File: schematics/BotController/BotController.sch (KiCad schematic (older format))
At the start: 15 parts, among them IC1 ATMEGA644-P, SW2 reset, X1 CRYSTAL_OSSCI

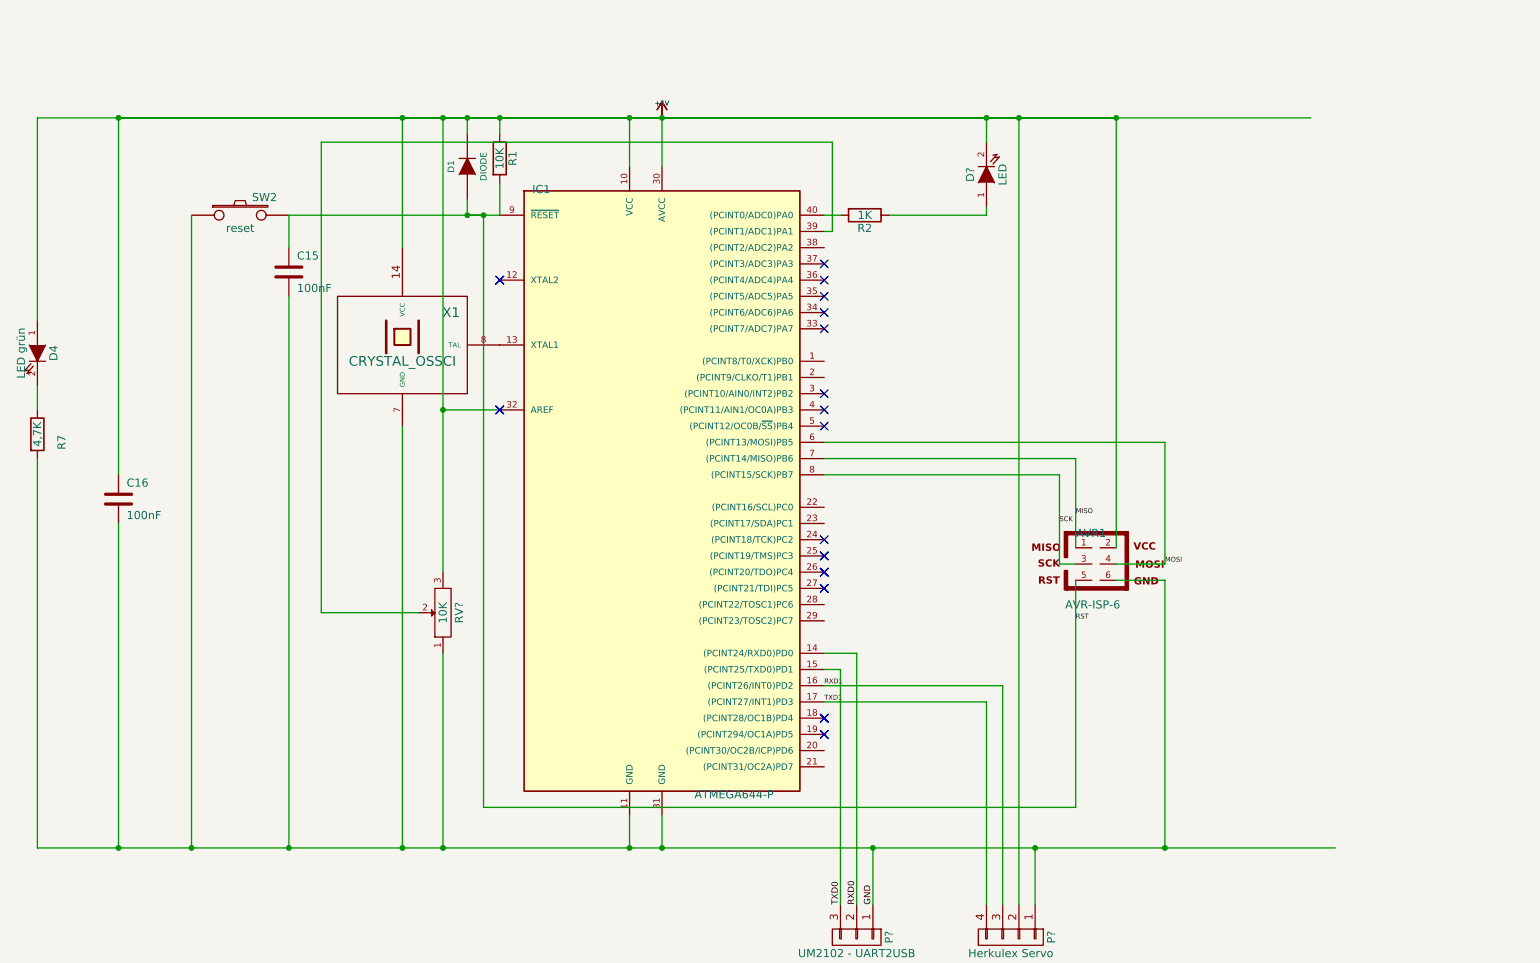
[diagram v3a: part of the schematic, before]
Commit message: Rotary Encoder mit gleicher I2c Adresse angesprochen
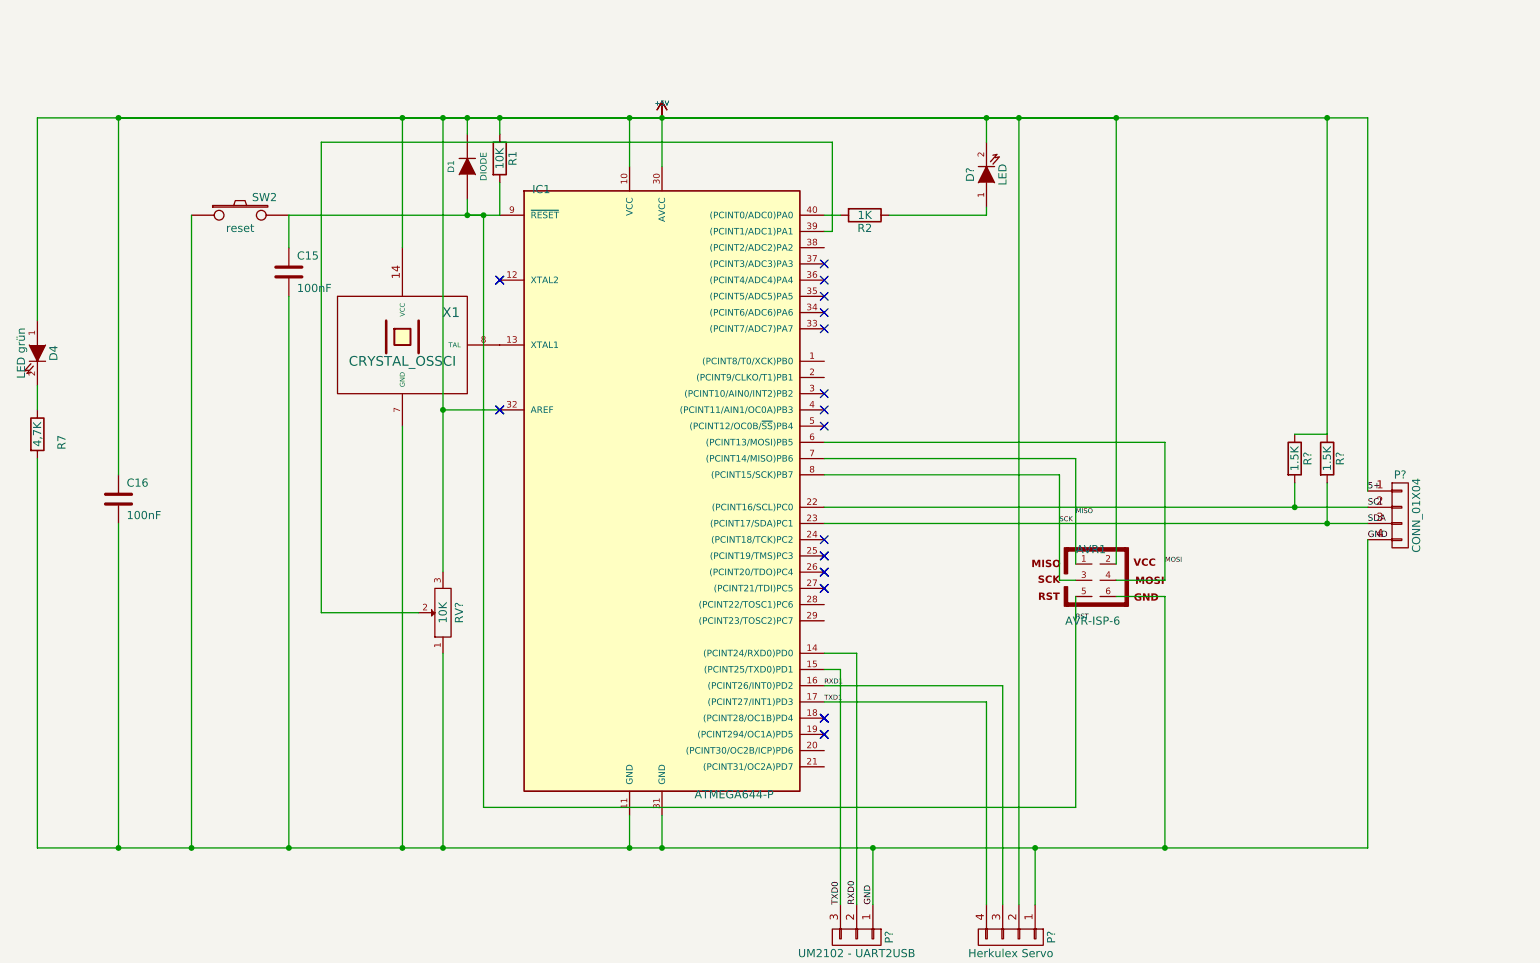
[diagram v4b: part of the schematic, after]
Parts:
- added P?: CONN_01X04, symbol CONN_01X04
- added R? (x2): 1.5K, symbol R
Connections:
- net labels added: 5+, SCl, SDA
- wire segments 63 -> 105
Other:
- moved on the sheet: AVR1
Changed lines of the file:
@@
 	2750 2300 2750 2500
 Wire Wire Line
-	2750 2300 4050 2300
+	2750 2300 3850 2300
+Wire Wire Line
+	3850 2300 3950 2300
+Wire Wire Line
+	3950 2300 4050 2300
 Wire Wire Line
 	3950 5950 7600 5950
 Wire Wire Line
-	7600 5950 7600 4550
-Wire Wire Line
-	7850 4550 8150 4550
+	7600 5950 7600 4650
+Wire Wire Line
+	7850 4650 8150 4650
 Connection ~ 3950 2300
 Wire Wire Line
@@
 	8150 3700 6050 3700
 Wire Wire Line
-	7850 1700 7850 4350
+	7850 1700 7850 4450
 Wire Wire Line
 	3950 5950 3950 2300
@@
 Connection ~ 2750 6200
 Wire Wire Line
-	7600 3800 7600 4350
-Wire Wire Line
-	8150 4450 8150 3700
+	7600 3800 7600 4450
+Wire Wire Line
+	8150 3700 8150 4550
 Wire Wire Line
 	1200 3350 1200 3500
@@
 $EndComp
 Wire Wire Line
-	1200 1700 9050 1700
+	1200 1700 1700 1700
+Wire Wire Line
+	1700 1700 3450 1700
+Wire Wire Line
+	3450 1700 3700 1700
+Wire Wire Line
+	3700 1700 3850 1700
+Wire Wire Line
+	3850 1700 4050 1700
+Wire Wire Line
+	4050 1700 4850 1700
+Wire Wire Line
+	4850 1700 5050 1700
+Wire Wire Line
+	5050 1700 7050 1700
+Wire Wire Line
+	7050 1700 7250 1700
+Wire Wire Line
+	7250 1700 7850 1700
+Wire Wire Line
+	7850 1700 9150 1700
+Wire Wire Line
+	9150 1700 9400 1700
 Wire Wire Line
 	4050 1700 4050 1800
 Connection ~ 7850 1700
 Wire Wire Line
-	8150 4550 8150 6200
+	8150 4650 8150 6200
 Wire Wire Line
 	3850 2200 3850 2300
@@
 	3850 2300 3950 2300
 Wire Wire Line
-	1700 1700 7850 1700
+	1700 1700 3450 1700
+Wire Wire Line
+	3450 1700 3700 1700
+Wire Wire Line
+	3700 1700 3850 1700
+Wire Wire Line
+	3850 1700 4050 1700
+Wire Wire Line
+	4050 1700 4850 1700
+Wire Wire Line
+	4850 1700 5050 1700
+Wire Wire Line
+	5050 1700 7050 1700
+Wire Wire Line
+	7050 1700 7250 1700
+Wire Wire Line
+	7250 1700 7850 1700
 NoConn ~ 6050 2600
 NoConn ~ 6050 5500
@@
 L AVR-ISP-6 AVR1
 U 1 1 50E5677B
-P 7750 4450
-F 0 "AVR1" H 7695 4640 50  0000 C CNN
-F 1 "AVR-ISP-6" H 7535 4170 50  0000 L BNN
-F 2 "AVR-ISP-6" V 7255 4440 50  0001 C CNN
-F 3 "" H 7750 4450 60  0001 C CNN
-	1    7750 4450
-	1    0    0    -1
-$EndComp
-Wire Wire Line
-	7850 4450 8150 4450
-Wire Wire Line
-	7600 4450 7500 4450
-Wire Wire Line
-	7500 4450 7500 3900
+P 7750 4550
+F 0 "AVR1" H 7695 4740 50  0000 C CNN
+F 1 "AVR-ISP-6" H 7535 4270 50  0000 L BNN
+F 2 "AVR-ISP-6" V 7255 4540 50  0001 C CNN
+F 3 "" H 7750 4550 60  0001 C CNN
+	1    7750 4550
+	1    0    0    -1
+$EndComp
+Wire Wire Line
+	8150 4550 7850 4550
+Wire Wire Line
+	7500 4550 7600 4550
+Wire Wire Line
+	7500 3900 7500 4550
 Wire Wire Line
 	7500 3900 6050 3900
 Wire Wire Line
-	1200 6200 9200 6200
+	1200 6200 1700 6200
+Wire Wire Line
+	1700 6200 2150 6200
+Wire Wire Line
+	2150 6200 2750 6200
+Wire Wire Line
+	2750 6200 3450 6200
+Wire Wire Line
+	3450 6200 3700 6200
+Wire Wire Line
+	3700 6200 4850 6200
+Wire Wire Line
+	4850 6200 5050 6200
+Wire Wire Line
+	5050 6200 6350 6200
+Wire Wire Line
+	6350 6200 7350 6200
+Wire Wire Line
+	7350 6200 8150 6200
+Wire Wire Line
+	8150 6200 9400 6200
 $Comp
 L SW_PUSH SW2
@@
 	4050 3500 3700 3500
 Wire Wire Line
-	3700 1700 3700 4500
+	3700 1700 3700 3500
+Wire Wire Line
+	3700 3500 3700 4500
 Wire Wire Line
 	3700 5000 3700 6200
@@
 Wire Wire Line
 	7050 5300 7050 6550
+Wire Wire Line
+	6050 4100 8950 4100
+Wire Wire Line
+	8950 4100 9400 4100
+Wire Wire Line
+	6050 4200 9150 4200
+Wire Wire Line
+	9150 4200 9400 4200
+Text Label 9400 4100 0    39   ~ 0
+SCl
+Text Label 9400 4200 0    39   ~ 0
+SDA
+Wire Wire Line
+	9400 6200 9400 4300
+$Comp
+L R R?
+U 1 1 5727190E
+P 8950 3800
+F 0 "R?" V 9030 3800 50  0000 C CNN
+F 1 "1.5K" V 8950 3800 50  0000 C CNN
+F 2 "" V 8880 3800 30  0000 C CNN
+F 3 "" H 8950 3800 30  0000 C CNN
+	1    8950 3800
+	1    0    0    -1
+$EndComp
+$Comp
+L R R?
+U 1 1 57271C02
+P 9150 3800
+F 0 "R?" V 9230 3800 50  0000 C CNN
+F 1 "1.5K" V 9150 3800 50  0000 C CNN
+F 2 "" V 9080 3800 30  0000 C CNN
+F 3 "" H 9150 3800 30  0000 C CNN
+	1    9150 3800
+	1    0    0    -1
+$EndComp
+Wire Wire Line
+	8950 3950 8950 4100
+Connection ~ 8950 4100
+Wire Wire Line
+	9150 3950 9150 4200
+Connection ~ 9150 4200
+Wire Wire Line
+	8950 3650 9150 3650
+Wire Wire Line
+	9150 3650 9150 1700
+$Comp
+L CONN_01X04 P?
+U 1 1 572B216F
+P 9600 4150
+F 0 "P?" H 9600 4400 50  0000 C CNN
+F 1 "CONN_01X04" V 9700 4150 50  0000 C CNN
+F 2 "" H 9600 4150 60  0000 C CNN
+F 3 "" H 9600 4150 60  0000 C CNN
+	1    9600 4150
+	1    0    0    -1
+$EndComp
+Wire Wire Line
+	9400 1700 9400 4000
+Connection ~ 9150 1700
+Text Label 9400 4300 0    39   ~ 0
+GND
+Text Label 9400 4000 0    39   ~ 0
+5+
 $EndSCHEMATC

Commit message: Neuer Schlanker Ellenbogen
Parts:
- added P?: Encoder Socket 0, symbol CONN_01X04
- P?: value CONN_01X04 -> Encoder Socket
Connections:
- net SCK: now also P?.2 (P2)
- net SCl: now also P?.1 (P1)
- net ConflictEncoderGND: now reaches IC1.1 ((PCINT8/T0/XCK)PB0)
- net ConflictEncoderGND: now also P?.4 (P4)
- net ConflictEncoderVDD: now reaches IC1.2 ((PCINT9/CLKO/T1)PB1)
- net ConflictEncoderVDD: now also P?.3 (P3)
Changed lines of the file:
@@
 	2750 2300 2750 2500
 Wire Wire Line
-	2750 2300 3850 2300
-Wire Wire Line
-	3850 2300 3950 2300
-Wire Wire Line
-	3950 2300 4050 2300
+	2750 2300 4050 2300
 Wire Wire Line
 	3950 5950 7600 5950
@@
 $EndComp
 Wire Wire Line
-	1200 1700 1700 1700
-Wire Wire Line
-	1700 1700 3450 1700
-Wire Wire Line
-	3450 1700 3700 1700
-Wire Wire Line
-	3700 1700 3850 1700
-Wire Wire Line
-	3850 1700 4050 1700
-Wire Wire Line
-	4050 1700 4850 1700
-Wire Wire Line
-	4850 1700 5050 1700
-Wire Wire Line
-	5050 1700 7050 1700
-Wire Wire Line
-	7050 1700 7250 1700
-Wire Wire Line
-	7250 1700 7850 1700
-Wire Wire Line
-	7850 1700 9150 1700
-Wire Wire Line
-	9150 1700 9400 1700
+	1200 1700 9400 1700
 Wire Wire Line
 	4050 1700 4050 1800
@@
 	3850 2300 3950 2300
 Wire Wire Line
-	1700 1700 3450 1700
-Wire Wire Line
-	3450 1700 3700 1700
-Wire Wire Line
-	3700 1700 3850 1700
-Wire Wire Line
-	3850 1700 4050 1700
-Wire Wire Line
-	4050 1700 4850 1700
-Wire Wire Line
-	4850 1700 5050 1700
-Wire Wire Line
-	5050 1700 7050 1700
-Wire Wire Line
-	7050 1700 7250 1700
-Wire Wire Line
-	7250 1700 7850 1700
+	1700 1700 7850 1700
 NoConn ~ 6050 2600
 NoConn ~ 6050 5500
@@
 	7500 3900 6050 3900
 Wire Wire Line
-	1200 6200 1700 6200
-Wire Wire Line
-	1700 6200 2150 6200
-Wire Wire Line
-	2150 6200 2750 6200
-Wire Wire Line
-	2750 6200 3450 6200
-Wire Wire Line
-	3450 6200 3700 6200
-Wire Wire Line
-	3700 6200 4850 6200
-Wire Wire Line
-	4850 6200 5050 6200
-Wire Wire Line
-	5050 6200 6350 6200
-Wire Wire Line
-	6350 6200 7350 6200
-Wire Wire Line
-	7350 6200 8150 6200
-Wire Wire Line
-	8150 6200 9400 6200
+	1200 6200 9400 6200
 $Comp
 L SW_PUSH SW2
@@
 	4050 3500 3700 3500
 Wire Wire Line
-	3700 1700 3700 3500
-Wire Wire Line
-	3700 3500 3700 4500
+	3700 1700 3700 4500
 Wire Wire Line
 	3700 5000 3700 6200
@@
 	7050 5300 7050 6550
 Wire Wire Line
-	6050 4100 8950 4100
-Wire Wire Line
-	8950 4100 9400 4100
-Wire Wire Line
-	6050 4200 9150 4200
-Wire Wire Line
-	9150 4200 9400 4200
+	6050 4100 9400 4100
+Wire Wire Line
+	6050 4200 9400 4200
 Text Label 9400 4100 0    39   ~ 0
 SCl
@@
 P 9600 4150
 F 0 "P?" H 9600 4400 50  0000 C CNN
-F 1 "CONN_01X04" V 9700 4150 50  0000 C CNN
+F 1 "Encoder Socket" V 9700 4150 50  0000 C CNN
 F 2 "" H 9600 4150 60  0000 C CNN
 F 3 "" H 9600 4150 60  0000 C CNN
@@
 Text Label 9400 4000 0    39   ~ 0
 5+
+Wire Wire Line
+	6050 3200 8500 3200
+Text Label 6050 3300 0    39   ~ 0
+ConflictEncoderVDD
+Text Label 6050 3200 0    39   ~ 0
+ConflictEncoderGND
+$Comp
+L CONN_01X04 P?
+U 1 1 572B75C3
+P 8700 3050
+F 0 "P?" H 8700 3300 50  0000 C CNN
+F 1 "Encoder Socket 0" V 8800 3050 50  0000 C CNN
+F 2 "" H 8700 3050 60  0000 C CNN
+F 3 "" H 8700 3050 60  0000 C CNN
+	1    8700 3050
+	1    0    0    -1
+$EndComp
+Wire Wire Line
+	8500 3100 8150 3100
+Wire Wire Line
+	8150 3100 8150 3300
+Wire Wire Line
+	8150 3300 6050 3300
+Wire Wire Line
+	8500 3000 8400 3000
+Wire Wire Line
+	8400 3000 8400 4200
+Connection ~ 8400 4200
+Wire Wire Line
+	8500 2900 8300 2900
+Wire Wire Line
+	8300 2900 8300 4100
+Connection ~ 8300 4100
 $EndSCHEMATC

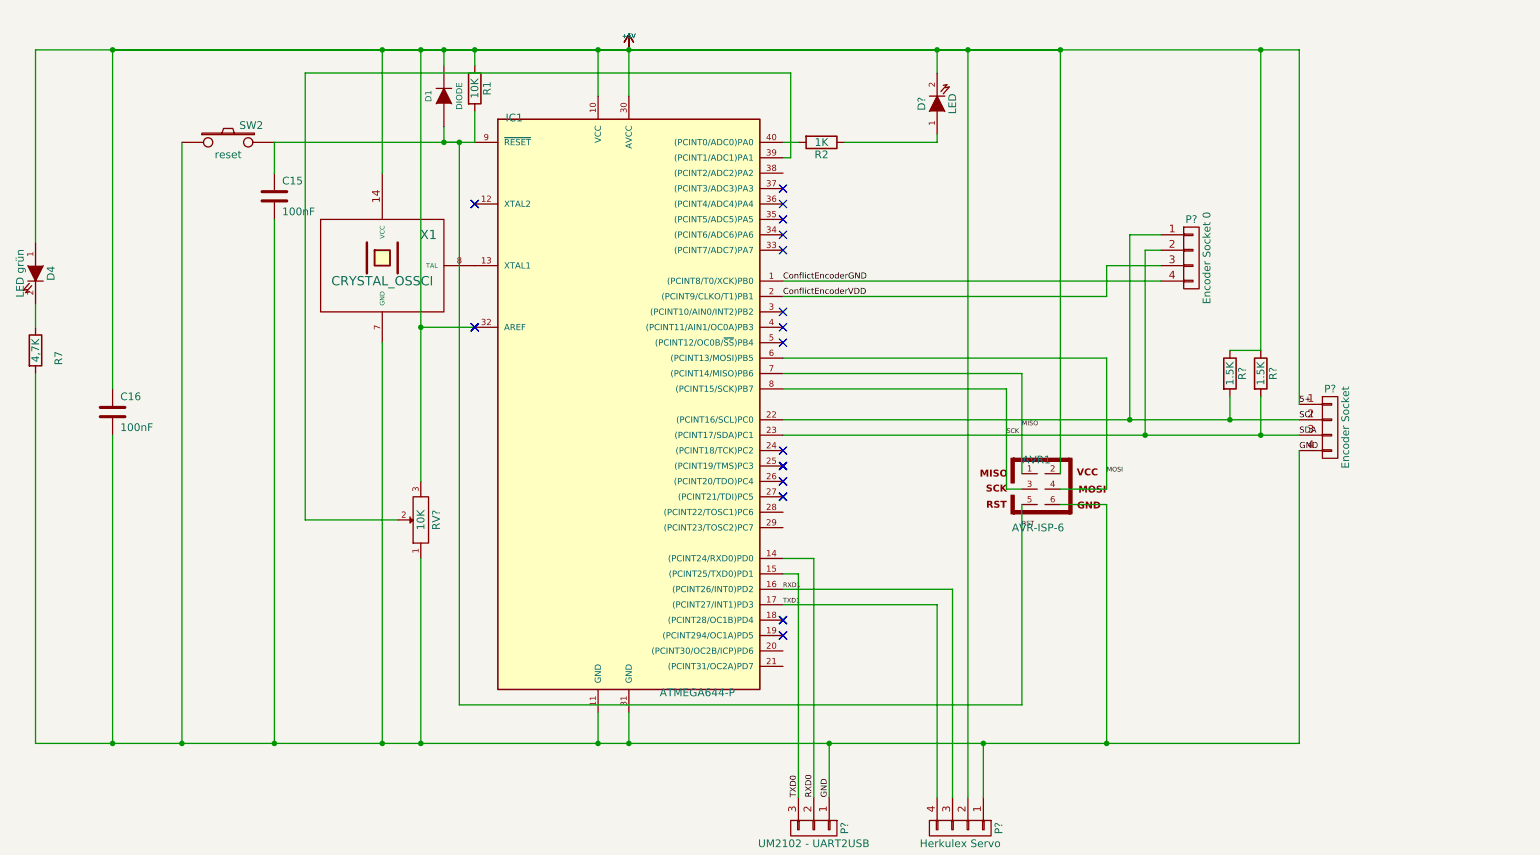
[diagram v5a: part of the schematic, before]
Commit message: Stepper control imroved
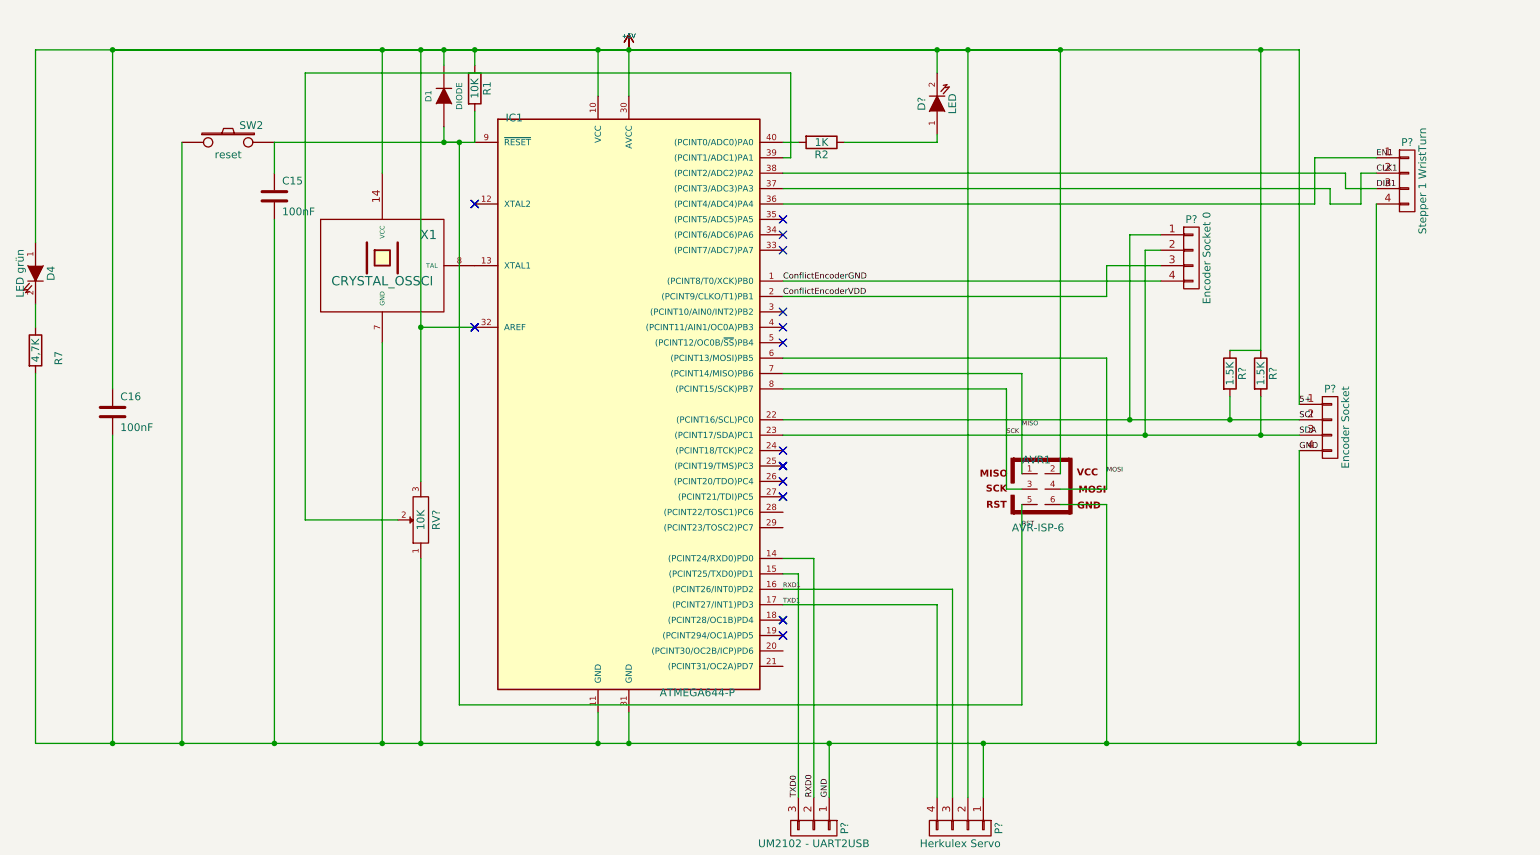
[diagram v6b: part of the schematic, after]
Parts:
- added P?: Stepper 1 WristTurn, symbol CONN_01X04
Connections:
- net GND: now also P?.4 (P4)
- net EN1: now reaches IC1.36 ((PCINT4/ADC4)PA4)
- net EN1: now also P?.1 (P1)
- net CLK1: now reaches IC1.37 ((PCINT3/ADC3)PA3)
- net CLK1: now also P?.2 (P2)
- net DIR1: now reaches IC1.38 ((PCINT2/ADC2)PA2)
- net DIR1: now also P?.3 (P3)
- no-connect marks 25 -> 23
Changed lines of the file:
@@
 Wire Wire Line
 	1700 1700 7850 1700
-NoConn ~ 6050 2600
 NoConn ~ 6050 5500
 $Comp
@@
 NoConn ~ 6050 2900
 NoConn ~ 6050 2800
-NoConn ~ 6050 2700
 NoConn ~ 6050 3000
 NoConn ~ 6050 5400
@@
 	7500 3900 6050 3900
 Wire Wire Line
-	1200 6200 9400 6200
+	1200 6200 9900 6200
 $Comp
 L SW_PUSH SW2
@@
 	8300 2900 8300 4100
 Connection ~ 8300 4100
+$Comp
+L CONN_01X04 P?
+U 1 1 572E5E87
+P 10100 2550
+F 0 "P?" H 10100 2800 50  0000 C CNN
+F 1 "Stepper 1 WristTurn" V 10200 2550 50  0000 C CNN
+F 2 "" H 10100 2550 60  0000 C CNN
+F 3 "" H 10100 2550 60  0000 C CNN
+	1    10100 2550
+	1    0    0    -1
+$EndComp
+Wire Wire Line
+	9900 6200 9900 2700
+Connection ~ 9400 6200
+Text Label 9900 2600 0    39   ~ 0
+DIR1
+Text Label 9900 2500 0    39   ~ 0
+CLK1
+Text Label 9900 2400 0    39   ~ 0
+EN1
+Wire Wire Line
+	9700 2500 6050 2500
+Wire Wire Line
+	9900 2600 9700 2600
+Wire Wire Line
+	9700 2600 9700 2500
+Wire Wire Line
+	9900 2500 9800 2500
+Wire Wire Line
+	9800 2500 9800 2700
+Wire Wire Line
+	9800 2700 9600 2700
+Wire Wire Line
+	9600 2700 9600 2600
+Wire Wire Line
+	9600 2600 6050 2600
+Wire Wire Line
+	6050 2700 9500 2700
+Wire Wire Line
+	9500 2700 9500 2400
+Wire Wire Line
+	9500 2400 9900 2400
 $EndSCHEMATC
